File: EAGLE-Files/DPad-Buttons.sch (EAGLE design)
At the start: 1 part

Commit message: Updated board layouts
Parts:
- added JP2, JP3, JP4: (no value), pinhead:PINHD-1X1
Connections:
- net GND: now also JP2.1, JP3.1, JP4.1
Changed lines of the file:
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@@
 <part name="JP1" library="pinhead" library_urn="urn:adsk.eagle:library:325" deviceset="PINHD-1X5" device="/90" package3d_urn="urn:adsk.eagle:package:22467/2"/>
 <part name="GND1" library="supply1" library_urn="urn:adsk.eagle:library:371" deviceset="GND" device=""/>
+<part name="JP2" library="pinhead" library_urn="urn:adsk.eagle:library:325" deviceset="PINHD-1X1" device="" package3d_urn="urn:adsk.eagle:package:22485/2"/>
+<part name="GND2" library="supply1" library_urn="urn:adsk.eagle:library:371" deviceset="GND" device=""/>
+<part name="JP3" library="pinhead" library_urn="urn:adsk.eagle:library:325" deviceset="PINHD-1X1" device="" package3d_urn="urn:adsk.eagle:package:22485/2"/>
+<part name="GND3" library="supply1" library_urn="urn:adsk.eagle:library:371" deviceset="GND" device=""/>
+<part name="JP4" library="pinhead" library_urn="urn:adsk.eagle:library:325" deviceset="PINHD-1X1" device="" package3d_urn="urn:adsk.eagle:package:22485/2"/>
+<part name="GND4" library="supply1" library_urn="urn:adsk.eagle:library:371" deviceset="GND" device=""/>
 </parts>
 <sheets>
@@
 <attribute name="VALUE" x="71.12" y="50.8" size="1.778" layer="96" rot="R270"/>
 </instance>
+<instance part="JP2" gate="G$1" x="60.96" y="58.42" smashed="yes" rot="R90">
+<attribute name="NAME" x="57.785" y="52.07" size="1.778" layer="95" rot="R90"/>
+<attribute name="VALUE" x="66.04" y="52.07" size="1.778" layer="96" rot="R90"/>
+</instance>
+<instance part="GND2" gate="1" x="60.96" y="48.26" smashed="yes">
+<attribute name="VALUE" x="58.42" y="45.72" size="1.778" layer="96"/>
+</instance>
+<instance part="JP3" gate="G$1" x="53.34" y="58.42" smashed="yes" rot="R90">
+<attribute name="NAME" x="50.165" y="52.07" size="1.778" layer="95" rot="R90"/>
+<attribute name="VALUE" x="58.42" y="52.07" size="1.778" layer="96" rot="R90"/>
+</instance>
+<instance part="GND3" gate="1" x="53.34" y="48.26" smashed="yes">
+<attribute name="VALUE" x="50.8" y="45.72" size="1.778" layer="96"/>
+</instance>
+<instance part="JP4" gate="G$1" x="45.72" y="58.42" smashed="yes" rot="R90">
+<attribute name="NAME" x="42.545" y="52.07" size="1.778" layer="95" rot="R90"/>
+<attribute name="VALUE" x="50.8" y="52.07" size="1.778" layer="96" rot="R90"/>
+</instance>
+<instance part="GND4" gate="1" x="45.72" y="48.26" smashed="yes">
+<attribute name="VALUE" x="43.18" y="45.72" size="1.778" layer="96"/>
+</instance>
 </instances>
 <busses>
@@
 <wire x1="76.2" y1="48.26" x2="86.36" y2="48.26" width="0.1524" layer="91"/>
 </segment>
+<segment>
+<pinref part="JP2" gate="G$1" pin="1"/>
+<pinref part="GND2" gate="1" pin="GND"/>
+<wire x1="60.96" y1="55.88" x2="60.96" y2="50.8" width="0.1524" layer="91"/>
+</segment>
+<segment>
+<pinref part="JP3" gate="G$1" pin="1"/>
+<pinref part="GND3" gate="1" pin="GND"/>
+<wire x1="53.34" y1="55.88" x2="53.34" y2="50.8" width="0.1524" layer="91"/>
+</segment>
+<segment>
+<pinref part="JP4" gate="G$1" pin="1"/>
+<pinref part="GND4" gate="1" pin="GND"/>
+<wire x1="45.72" y1="55.88" x2="45.72" y2="50.8" width="0.1524" layer="91"/>
+</segment>
 </net>

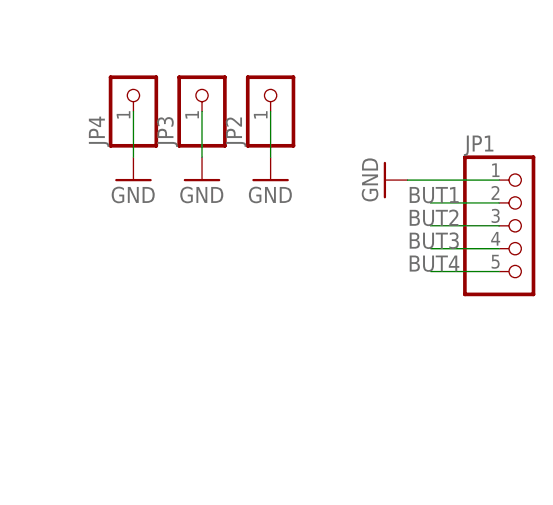
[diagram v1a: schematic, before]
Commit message: Updated the DPad and Four Buttons PCB designs for production
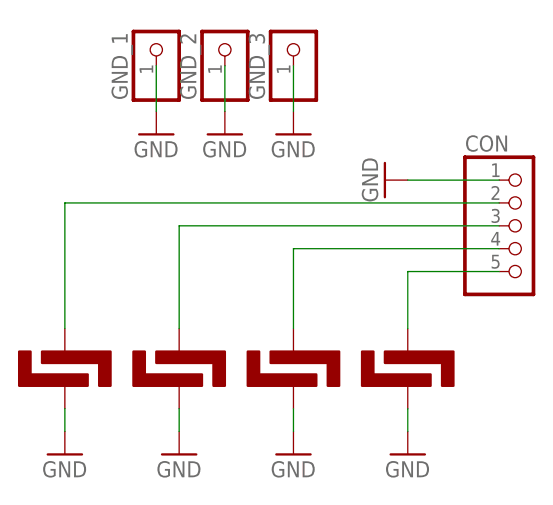
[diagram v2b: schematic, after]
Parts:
- removed JP2, JP3, JP4: (no value), pinhead:PINHD-1X1
- added BTN1, BTN2, BTN3, BTN4: BTN_5MM_LONG, surfacebuttons:BTN_5MM_LONG
- added GND_1, GND_2, GND_3: (no value), pinhead:PINHD-1X1
- renumbered JP1 to CON
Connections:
- removed net BUT1: CON.2
- removed net BUT2: CON.3
- removed net BUT3: CON.4
- removed net BUT4: CON.5
- new net N$1: BTN1.P$1, CON.2
- new net N$2: BTN4.P$1, CON.5
- new net N$3: BTN3.P$1, CON.4
- new net N$4: BTN2.P$1, CON.3
- net GND: now also BTN1.P$2, BTN2.P$2, BTN3.P$2, BTN4.P$2, GND_1.1, GND_2.1, GND_3.1; no longer JP2.1, JP3.1, JP4.1
